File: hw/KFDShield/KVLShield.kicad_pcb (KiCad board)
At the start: 2 copper layers, 68.6 x 53.3 mm, 134 parts, among them J1 MR_Block, J2 OLED, J3 MR_Jack, P1 Power, P2 Analog, P3 Digital, P4 Digital, P5 CONN_01X01, P6 CONN_01X01, P7 CONN_01X01, P8 CONN_01X01, Q1 MMBT3904LT1G, Q2 MMBT3904LT1G, SW1 SW_Push, SW2 Up, SW3 Down, SW4 Enter

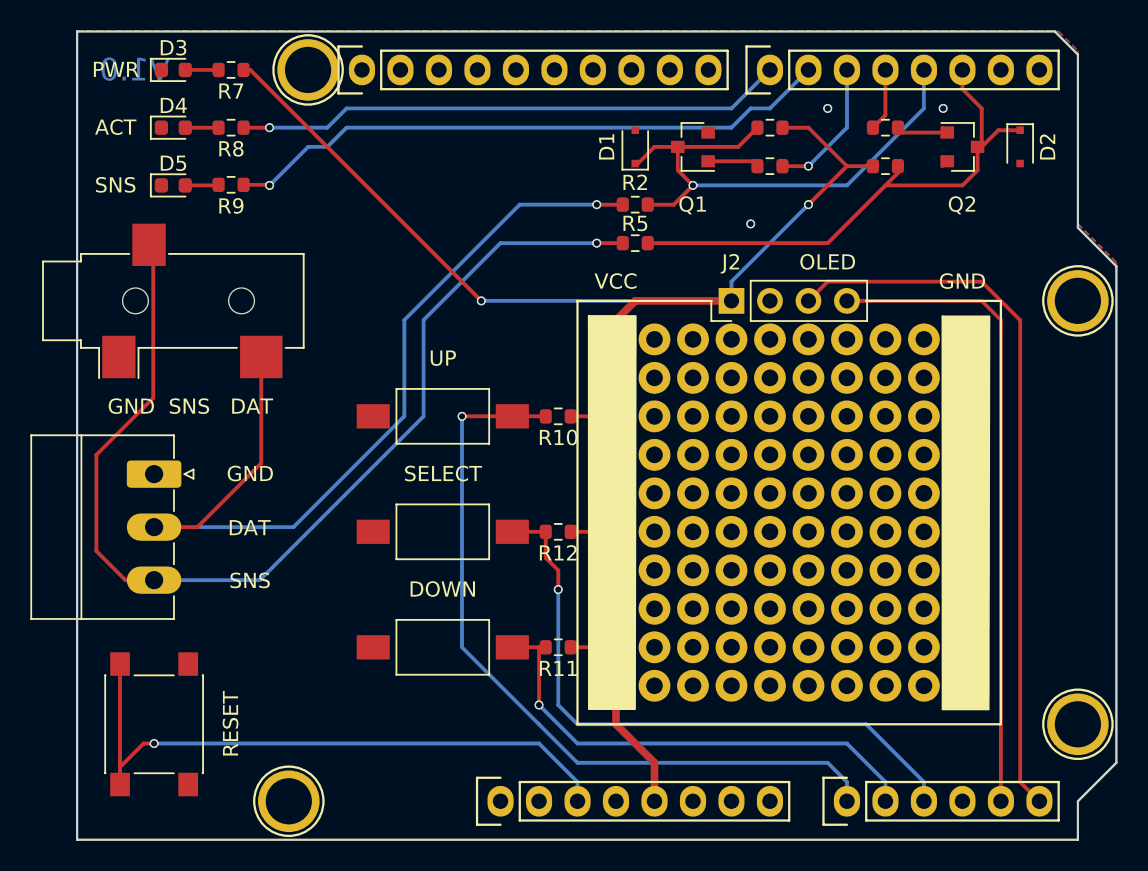
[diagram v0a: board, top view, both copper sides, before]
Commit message: recommended pcb updates
- got (almost) all traces on top layer
- increased trace widths
- moved around buttons to make trace routing cleaner
- added stitching vias to connect top/bottom ground pours
- moved gerbers to gerber directory, only exported necessary layers
- rearranged components for KFD signal lines for better routing

I think that's it
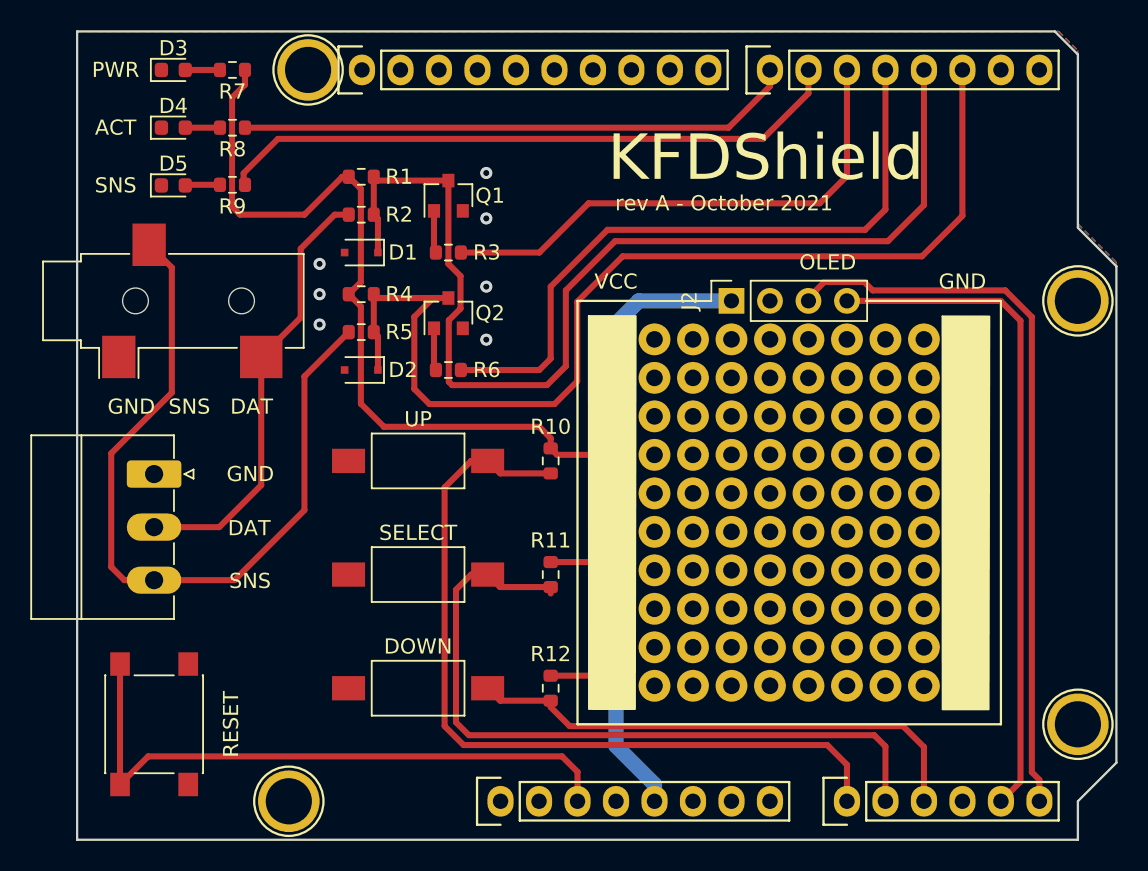
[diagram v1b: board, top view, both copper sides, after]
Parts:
- J2: footprint Connector_PinHeader_2.54mm:PinHeader_1x04_P2.54mm_Vertical -> Connector_PinSocket_2.54mm:PinSocket_1x04_P2.54mm_Vertical
- moved D2 45.9 mm to (129.7, 95.4), turned to 180 degrees
- moved Q2 35.6 mm to (135.5, 91.6), turned to 90 degrees
- moved R4 35.6 mm to (129.7, 90.4)
- moved R6 33.0 mm to (135.5, 95.4), turned to 180 degrees
- moved R1 27.2 mm to (129.7, 82.6), turned to 0 degrees
- moved R3 22.0 mm to (135.5, 87.6)
- moved D1 19.4 mm to (129.7, 87.6), turned to 180 degrees
- moved R5 19.0 mm to (129.7, 92.9)
- moved R2 18.1 mm to (129.7, 85.1)
- moved Q1 16.5 mm to (135.5, 83.9), turned to 90 degrees
- moved SW4 10.4 mm to (133.5, 116.4)
- moved R12 10.3 mm to (142.2, 116.4), turned to 270 degrees
- moved SW3 5.07 mm to (133.5, 108.9)
- moved R11 4.83 mm to (142.2, 108.9), turned to 270 degrees
- moved SW2 3.36 mm to (133.5, 101.4)
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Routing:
- net /4: track 4.15 -> 44.4 mm
- net /3(**): track 35.4 -> 72.3 mm, vias 1 -> 0
- net /2: track 35.9 -> 72.1 mm
- net /KFD_DATA: track 59.7 -> 29.4 mm, vias 1 -> 0
- net /5(**): track 9.12 -> 34.6 mm, vias 1 -> 0
- net /KFD_SENSE: track 71.3 -> 52.8 mm, vias 1 -> 0
- net /A1: track 31.8 -> 48.8 mm, vias 1 -> 0
- net /A2: track 41.5 -> 34.2 mm, vias 1 -> 0
- net +5V: track 107.5 -> 102.9 mm, vias 2 -> 0
- net /A0: track 51.1 -> 53.8 mm, vias 1 -> 0
- net /A4(SDA): track 42.4 -> 44.2 mm
- net /Reset: track 42.8 -> 41.3 mm, vias 1 -> 0
- net /6(**): track 40.4 -> 41.8 mm, vias 1 -> 0
- net Net-(Q2-Pad1): track 3.84 -> 2.80 mm
- net /A5(SCL): track 47.8 -> 48.5 mm
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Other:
- rule trace_min: 0.127 -> 0.2
- board text added: "KFDShield"
- board text added: "rev A - October 2021"
- board text removed: "V1.0"

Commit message: beta hw rev sent to fab house
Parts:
- J3: footprint Connector_Audio:Jack_3.5mm_CUI_SJ-3523-SMT_Horizontal -> Connector_Audio:Jack_3.5mm_PJ320D_Horizontal
- SW2, SW3, SW4: footprint Button_Switch_SMD:SW_SPST_FSMSM -> Button_Switch_SMD:SW_SPST_CK_RS282G05A3
- turned J3 to 0 degrees
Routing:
- net /KFD_DATA: track 29.4 -> 34.1 mm
- net /KFD_SENSE: track 52.8 -> 51.4 mm
- net GND: vias 7 -> 11
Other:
- board text added: "rev A - November 2021"
- board text removed: "rev A - October 2021"
